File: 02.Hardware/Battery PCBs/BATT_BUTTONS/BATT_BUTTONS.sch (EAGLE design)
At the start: 4 parts

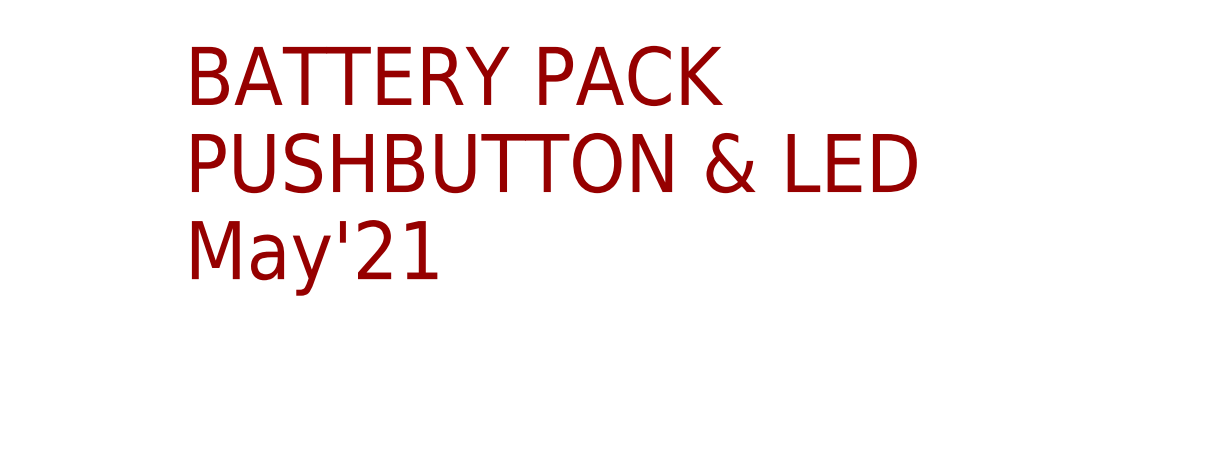
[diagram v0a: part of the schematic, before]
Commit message: Reorganizacion de directorios
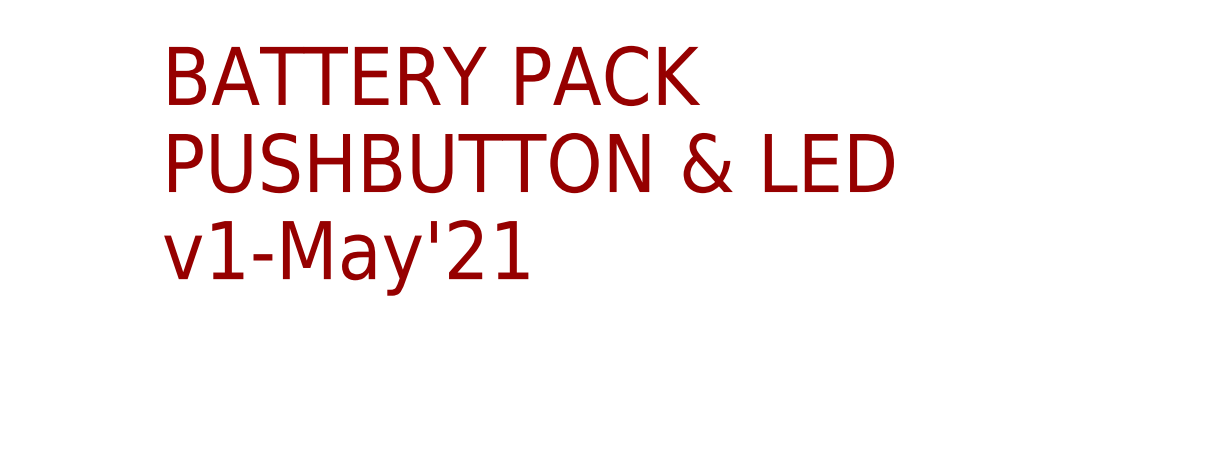
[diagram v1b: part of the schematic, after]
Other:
- note added: "BATTERY PACK PUSHBUTTON & LED v1-May'21"
- note removed: "BATTERY PACK PUSHBUTTON & LED May'21"
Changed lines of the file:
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@@
 <grid distance="0.1" unitdist="inch" unit="inch" style="lines" multiple="1" display="no" altdistance="0.01" altunitdist="inch" altunit="inch"/>
 <layers>
-<layer number="1" name="Top" color="4" fill="1" visible="yes" active="no"/>
-<layer number="2" name="Route2" color="16" fill="1" visible="yes" active="no"/>
-<layer number="3" name="Route3" color="17" fill="1" visible="yes" active="no"/>
-<layer number="4" name="Route4" color="18" fill="1" visible="yes" active="no"/>
-<layer number="5" name="Route5" color="19" fill="1" visible="yes" active="no"/>
-<layer number="6" name="Route6" color="25" fill="1" visible="yes" active="no"/>
-<layer number="7" name="Route7" color="26" fill="1" visible="yes" active="no"/>
-<layer number="8" name="Route8" color="27" fill="1" visible="yes" active="no"/>
-<layer number="9" name="Route9" color="28" fill="1" visible="yes" active="no"/>
-<layer number="10" name="Route10" color="29" fill="1" visible="yes" active="no"/>
-<layer number="11" name="Route11" color="30" fill="1" visible="yes" active="no"/>
-<layer number="12" name="Route12" color="20" fill="1" visible="yes" active="no"/>
-<layer number="13" name="Route13" color="21" fill="1" visible="yes" active="no"/>
-<layer number="14" name="Route14" color="22" fill="1" visible="yes" active="no"/>
-<layer number="15" name="Route15" color="23" fill="1" visible="yes" active="no"/>
-<layer number="16" name="Bottom" color="1" fill="1" visible="yes" active="no"/>
-<layer number="17" name="Pads" color="2" fill="1" visible="yes" active="no"/>
-<layer number="18" name="Vias" color="2" fill="1" visible="yes" active="no"/>
-<layer number="19" name="Unrouted" color="6" fill="1" visible="yes" active="no"/>
-<layer number="20" name="Dimension" color="24" fill="1" visible="yes" active="no"/>
-<layer number="21" name="tPlace" color="7" fill="1" visible="yes" active="no"/>
-<layer number="22" name="bPlace" color="7" fill="1" visible="yes" active="no"/>
-<layer number="23" name="tOrigins" color="15" fill="1" visible="yes" active="no"/>
-<layer number="24" name="bOrigins" color="15" fill="1" visible="yes" active="no"/>
-<layer number="25" name="tNames" color="7" fill="1" visible="yes" active="no"/>
-<layer number="26" name="bNames" color="7" fill="1" visible="yes" active="no"/>
-<layer number="27" name="tValues" color="7" fill="1" visible="yes" active="no"/>
-<layer number="28" name="bValues" color="7" fill="1" visible="yes" active="no"/>
+<layer number="1" name="Top" color="4" fill="1" visible="no" active="no"/>
+<layer number="2" name="Route2" color="16" fill="1" visible="no" active="no"/>
+<layer number="3" name="Route3" color="17" fill="1" visible="no" active="no"/>
+<layer number="4" name="Route4" color="18" fill="1" visible="no" active="no"/>
+<layer number="5" name="Route5" color="19" fill="1" visible="no" active="no"/>
+<layer number="6" name="Route6" color="25" fill="1" visible="no" active="no"/>
+<layer number="7" name="Route7" color="26" fill="1" visible="no" active="no"/>
+<layer number="8" name="Route8" color="27" fill="1" visible="no" active="no"/>
+<layer number="9" name="Route9" color="28" fill="1" visible="no" active="no"/>
+<layer number="10" name="Route10" color="29" fill="1" visible="no" active="no"/>
+<layer number="11" name="Route11" color="30" fill="1" visible="no" active="no"/>
+<layer number="12" name="Route12" color="20" fill="1" visible="no" active="no"/>
+<layer number="13" name="Route13" color="21" fill="1" visible="no" active="no"/>
+<layer number="14" name="Route14" color="22" fill="1" visible="no" active="no"/>
+<layer number="15" name="Route15" color="23" fill="1" visible="no" active="no"/>
+<layer number="16" name="Bottom" color="1" fill="1" visible="no" active="no"/>
+<layer number="17" name="Pads" color="2" fill="1" visible="no" active="no"/>
+<layer number="18" name="Vias" color="2" fill="1" visible="no" active="no"/>
+<layer number="19" name="Unrouted" color="6" fill="1" visible="no" active="no"/>
+<layer number="20" name="Dimension" color="24" fill="1" visible="no" active="no"/>
+<layer number="21" name="tPlace" color="7" fill="1" visible="no" active="no"/>
+<layer number="22" name="bPlace" color="7" fill="1" visible="no" active="no"/>
+<layer number="23" name="tOrigins" color="15" fill="1" visible="no" active="no"/>
+<layer number="24" name="bOrigins" color="15" fill="1" visible="no" active="no"/>
+<layer number="25" name="tNames" color="7" fill="1" visible="no" active="no"/>
+<layer number="26" name="bNames" color="7" fill="1" visible="no" active="no"/>
+<layer number="27" name="tValues" color="7" fill="1" visible="no" active="no"/>
+<layer number="28" name="bValues" color="7" fill="1" visible="no" active="no"/>
 <layer number="29" name="tStop" color="7" fill="3" visible="no" active="no"/>
 <layer number="30" name="bStop" color="7" fill="6" visible="no" active="no"/>
@@
 <layer number="35" name="tGlue" color="7" fill="4" visible="no" active="no"/>
 <layer number="36" name="bGlue" color="7" fill="5" visible="no" active="no"/>
-<layer number="37" name="tTest" color="7" fill="1" visible="yes" active="no"/>
-<layer number="38" name="bTest" color="7" fill="1" visible="yes" active="no"/>
+<layer number="37" name="tTest" color="7" fill="1" visible="no" active="no"/>
+<layer number="38" name="bTest" color="7" fill="1" visible="no" active="no"/>
 <layer number="39" name="tKeepout" color="4" fill="11" visible="no" active="no"/>
 <layer number="40" name="bKeepout" color="1" fill="11" visible="no" active="no"/>
@@
 <layer number="44" name="Drills" color="7" fill="1" visible="no" active="no"/>
 <layer number="45" name="Holes" color="7" fill="1" visible="no" active="no"/>
-<layer number="46" name="Milling" color="3" fill="1" visible="yes" active="no"/>
-<layer number="47" name="Measures" color="7" fill="1" visible="yes" active="no"/>
-<layer number="48" name="Document" color="7" fill="1" visible="yes" active="no"/>
-<layer number="49" name="Reference" color="7" fill="1" visible="yes" active="no"/>
-<layer number="50" name="dxf" color="7" fill="1" visible="yes" active="no"/>
-<layer number="51" name="tDocu" color="7" fill="1" visible="yes" active="no"/>
-<layer number="52" name="bDocu" color="7" fill="1" visible="yes" active="no"/>
-<layer number="53" name="tGND_GNDA" color="7" fill="9" visible="yes" active="no"/>
-<layer number="54" name="bGND_GNDA" color="1" fill="9" visible="yes" active="no"/>
-<layer number="56" name="wert" color="7" fill="1" visible="yes" active="no"/>
-<layer number="57" name="tCAD" color="7" fill="1" visible="yes" active="no"/>
-<layer number="59" name="tCarbon" color="7" fill="1" visible="yes" active="no"/>
-<layer number="60" name="bCarbon" color="7" fill="1" visible="yes" active="no"/>
+<layer number="46" name="Milling" color="3" fill="1" visible="no" active="no"/>
+<layer number="47" name="Measures" color="7" fill="1" visible="no" active="no"/>
+<layer number="48" name="Document" color="7" fill="1" visible="no" active="no"/>
+<layer number="49" name="Reference" color="7" fill="1" visible="no" active="no"/>
+<layer number="50" name="dxf" color="7" fill="1" visible="no" active="no"/>
+<layer number="51" name="tDocu" color="7" fill="1" visible="no" active="no"/>
+<layer number="52" name="bDocu" color="7" fill="1" visible="no" active="no"/>
+<layer number="53" name="tGND_GNDA" color="7" fill="9" visible="no" active="no"/>
+<layer number="54" name="bGND_GNDA" color="1" fill="9" visible="no" active="no"/>
+<layer number="56" name="wert" color="7" fill="1" visible="no" active="no"/>
+<layer number="57" name="tCAD" color="7" fill="1" visible="no" active="no"/>
+<layer number="59" name="tCarbon" color="7" fill="1" visible="no" active="no"/>
+<layer number="60" name="bCarbon" color="7" fill="1" visible="no" active="no"/>
 <layer number="88" name="SimResults" color="9" fill="1" visible="yes" active="yes"/>
 <layer number="89" name="SimProbes" color="9" fill="1" visible="yes" active="yes"/>
@@
 <description>INPUT</description>
 <plain>
-<text x="91.44" y="144.78" size="6.4516" layer="94" font="vector">BATTERY PACK
+<text x="88.9" y="144.78" size="6.4516" layer="94" font="vector">BATTERY PACK
 PUSHBUTTON &amp; LED
-May'21</text>
+v1-May'21</text>
 <wire x1="40.64" y1="111.76" x2="129.54" y2="111.76" width="0.1524" layer="94" style="longdash"/>
 <wire x1="129.54" y1="111.76" x2="220.98" y2="111.76" width="0.1524" layer="94" style="longdash"/>
